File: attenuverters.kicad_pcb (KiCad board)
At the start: 2 copper layers, 19 x 107.9 mm, 16 parts, among them J1 Power, J2 In1, J3 Out1, J4 In2, J5 Out2, U1 TL072

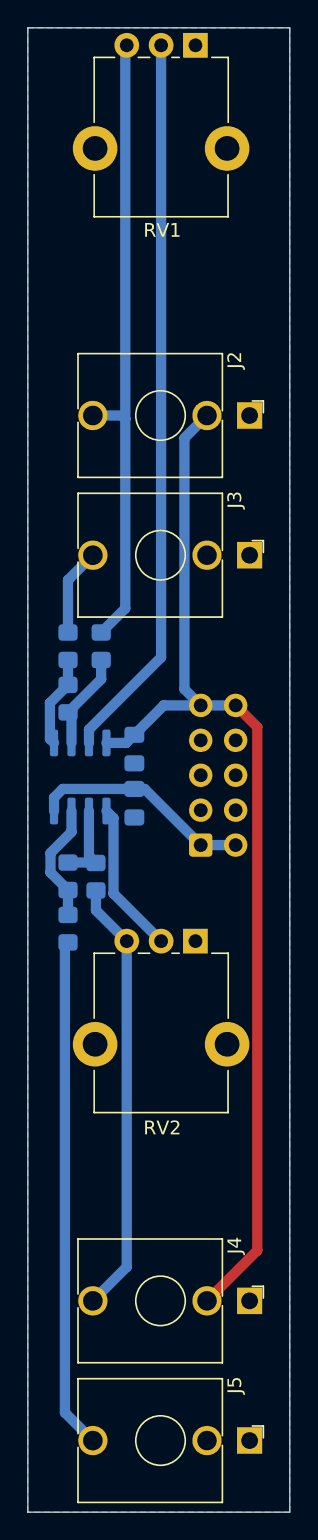
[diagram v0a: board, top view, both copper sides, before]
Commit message: Fixed power, updated KiCAD version
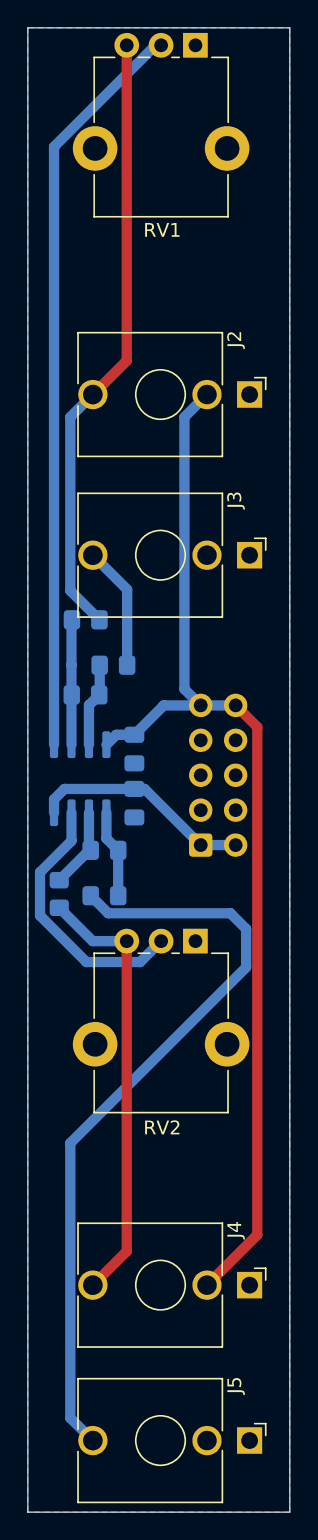
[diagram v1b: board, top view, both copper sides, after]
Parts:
- moved R3 3.58 mm to (38.0, 78.1), turned to 180 degrees
- moved R6 3.57 mm to (37.3, 94.9), turned to 0 degrees
- moved R4 3.26 mm to (37.3, 91.6), turned to 180 degrees
- moved R5 2.95 mm to (34.0, 94.7)
- moved R2 2.23 mm to (36.0, 74.8), turned to 0 degrees
- moved J2 1.52 mm to (47.9, 58.4)
- moved R1 1.30 mm to (35.9, 80.3), turned to 180 degrees
- moved J4 1.14 mm to (47.9, 123.2)
- moved U1 0.13 mm to (35.6, 86.4), turned to 90 degrees
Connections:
- J3 pad TN: Net-(J3-PadTN) -> unconnected-(J3-PadTN)
- J5 pad TN: Net-(J5-PadTN) -> unconnected-(J5-PadTN)
- R1 pad 2: Net-(R1-Pad2) -> Net-(U1B--)
- R2 pad 1: Net-(R1-Pad2) -> Net-(U1B--)
- R4 pad 2: Net-(R4-Pad2) -> Net-(U1A--)
- R5 pad 1: Net-(R4-Pad2) -> Net-(U1A--)
- RV1 pad 2: Net-(RV1-Pad2) -> Net-(U1B-+)
- RV2 pad 2: Net-(RV2-Pad2) -> Net-(U1A-+)
- U1 pad 1: Net-(R1-Pad1) -> Net-(R4-Pad1)
- U1 pad 2: Net-(R1-Pad2) -> Net-(U1A--)
- U1 pad 3: Net-(RV1-Pad2) -> Net-(U1A-+)
- U1 pad 4: +12V -> -12V
- U1 pad 5: Net-(RV2-Pad2) -> Net-(U1B-+)
- U1 pad 6: Net-(R4-Pad2) -> Net-(U1B--)
- U1 pad 7: Net-(R4-Pad1) -> Net-(R1-Pad1)
- U1 pad 8: -12V -> +12V
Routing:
- net Net-(U1B-+): track 0.00 -> 54.3 mm
- net Net-(RV1-Pad2): track 52.9 -> 0.00 mm
- net Net-(U1A-+): track 0.00 -> 19.3 mm
- net Net-(J5-PadT): track 37.2 -> 55.5 mm
- net Net-(RV2-Pad2): track 11.1 -> 0.00 mm
- net Net-(U1B--): track 0.00 -> 9.10 mm
- net Net-(R1-Pad2): track 7.14 -> 0.00 mm
- net Net-(R4-Pad2): track 6.04 -> 0.00 mm
- net Net-(U1A--): track 0.00 -> 5.97 mm
- net Net-(J3-PadT): track 6.37 -> 9.03 mm
- net Net-(R4-Pad1): track 8.72 -> 6.39 mm
- net Net-(J2-PadT): track 45.9 -> 44.5 mm
- net Net-(R1-Pad1): track 6.70 -> 6.10 mm
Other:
- net class Default removed
